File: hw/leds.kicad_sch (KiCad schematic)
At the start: 28 parts, among them Q4 SSM6N35AFE

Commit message: WIP; converging
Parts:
- removed D2101: DONb, LED_SMD:LED_0603_1608Metric, symbol Device:LED
- removed R25: 5k1, Resistor_SMD:R_0603_1608Metric, symbol Device:R_Small
- added D15: LED_Dual_RAG, proj_footprints:LED_Wuerth_Sideview, symbol Device:LED_Dual_KAK
- added R33, R34: 1k, Resistor_SMD:R_0603_1608Metric, symbol Device:R_Small
- D2101: value DONb -> FR_S
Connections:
- net LED_DONb is gone; now on net GND: Q4.4 (S)
- net +3V3: now also D15.2 (A); no longer Q4.5 (G)
- net at Q4.3 (D): now also R34.2
- new net: D15.1 (K1), R33.2
- new net: D15.3 (K2), R34.1
- new net LED_CDON: Q4.5 (G), R33.1
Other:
- note added: "Bi-color LED indicating power and FPGA config. complete: red: power, not configured grn: power, configured"
- moved on the sheet: D7, Q4A, Q4B, R10, R9, R98

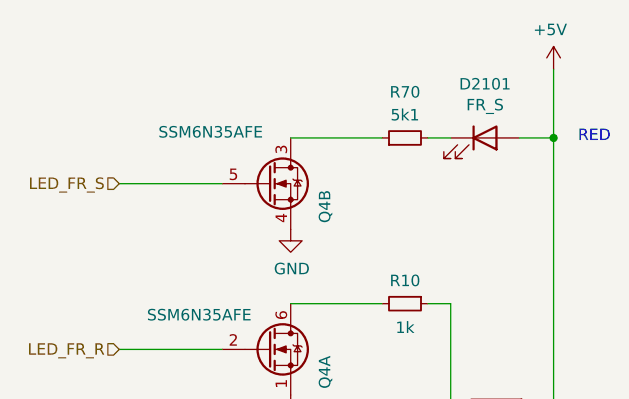
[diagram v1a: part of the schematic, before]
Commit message: updated some component values
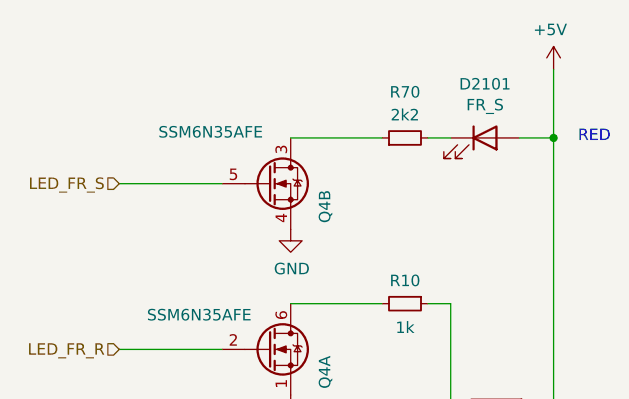
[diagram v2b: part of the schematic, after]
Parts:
- R70: value 5k1 -> 2k2
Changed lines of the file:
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@@
       (effects (font (size 1.27 1.27)))
     )
-    (property "Value" "5k1" (at 187.96 29.845 90)
+    (property "Value" "2k2" (at 187.96 29.845 90)
       (effects (font (size 1.27 1.27)))
     )

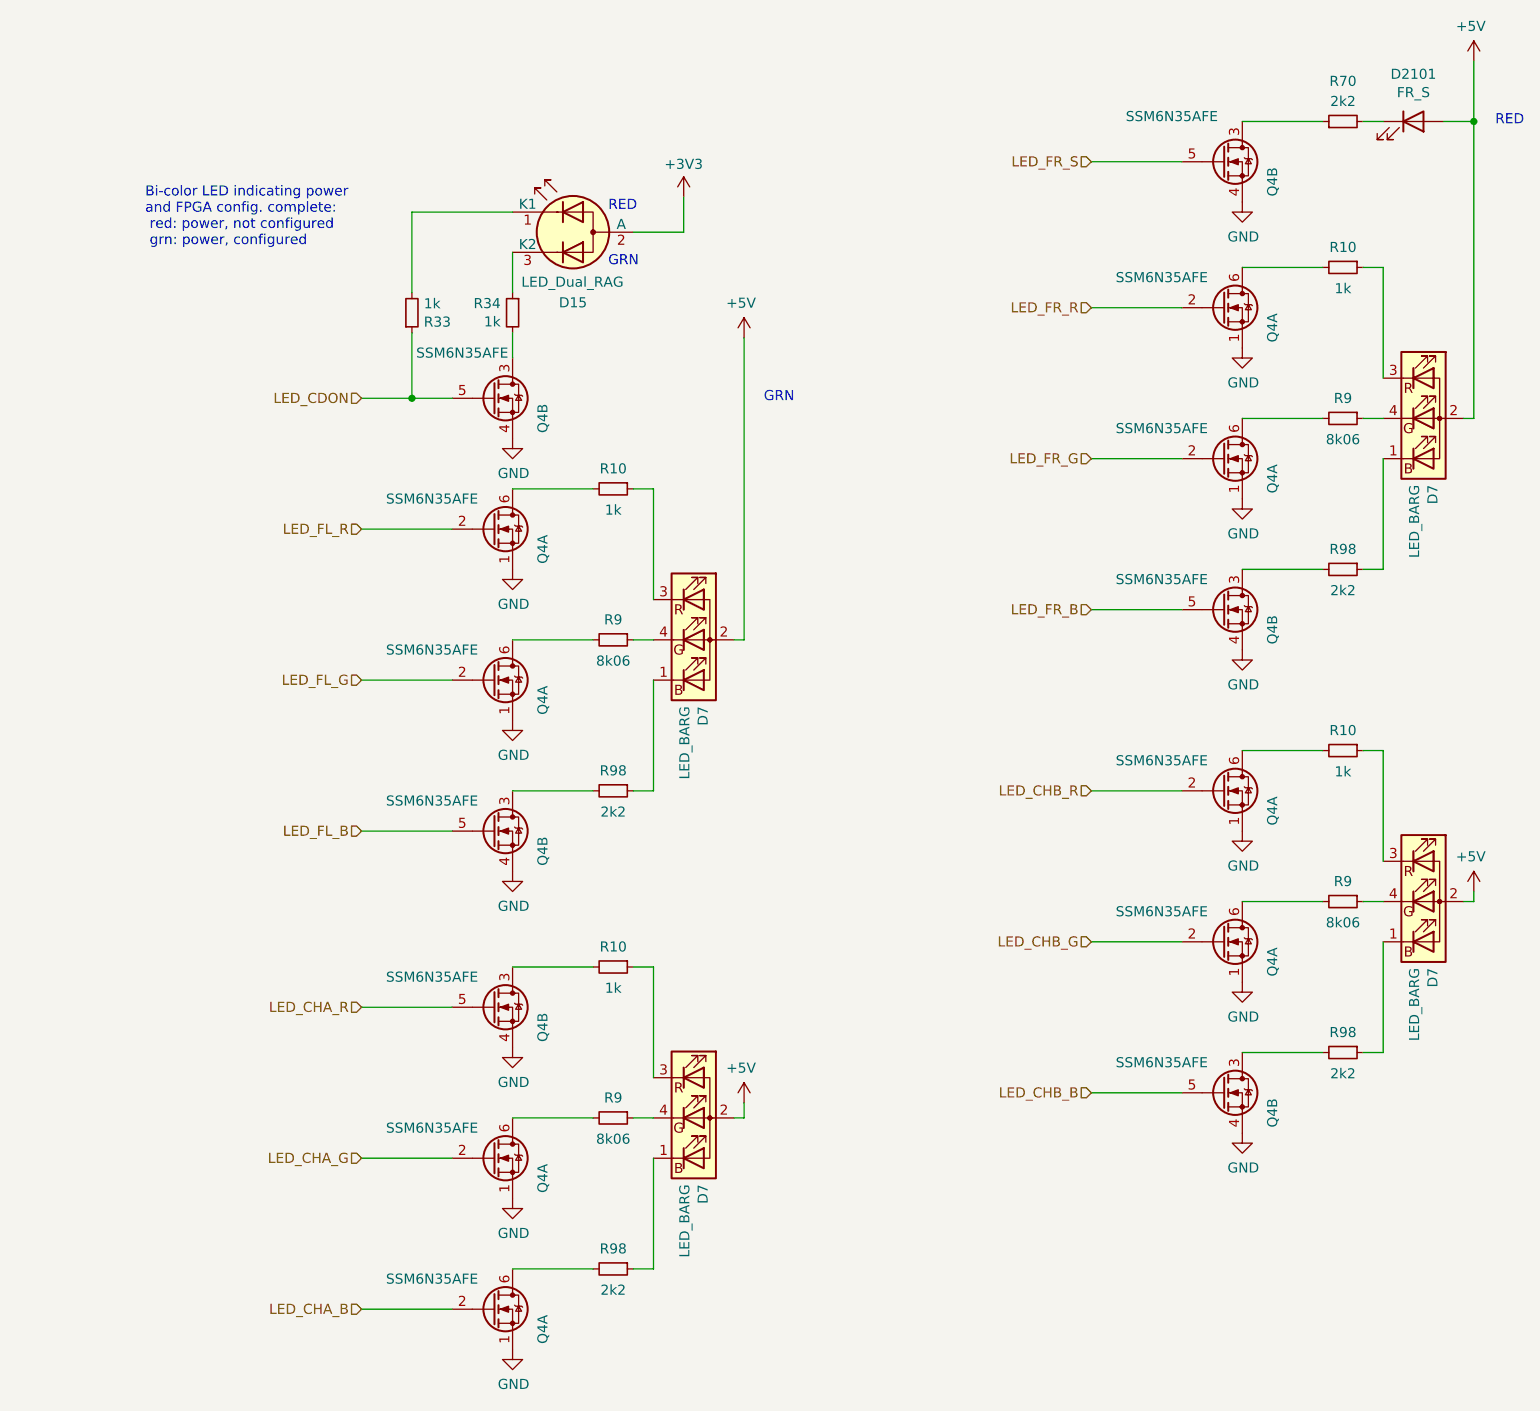
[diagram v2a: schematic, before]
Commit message: Moved LEDs from +5V to 3V3. Removed LED driver FETs.
NOTE: the 3V3 connection is provisional and needs to be
reworked along with the redesign of the 5V net.

The temporary connections exist just to satisfy DRC for now.
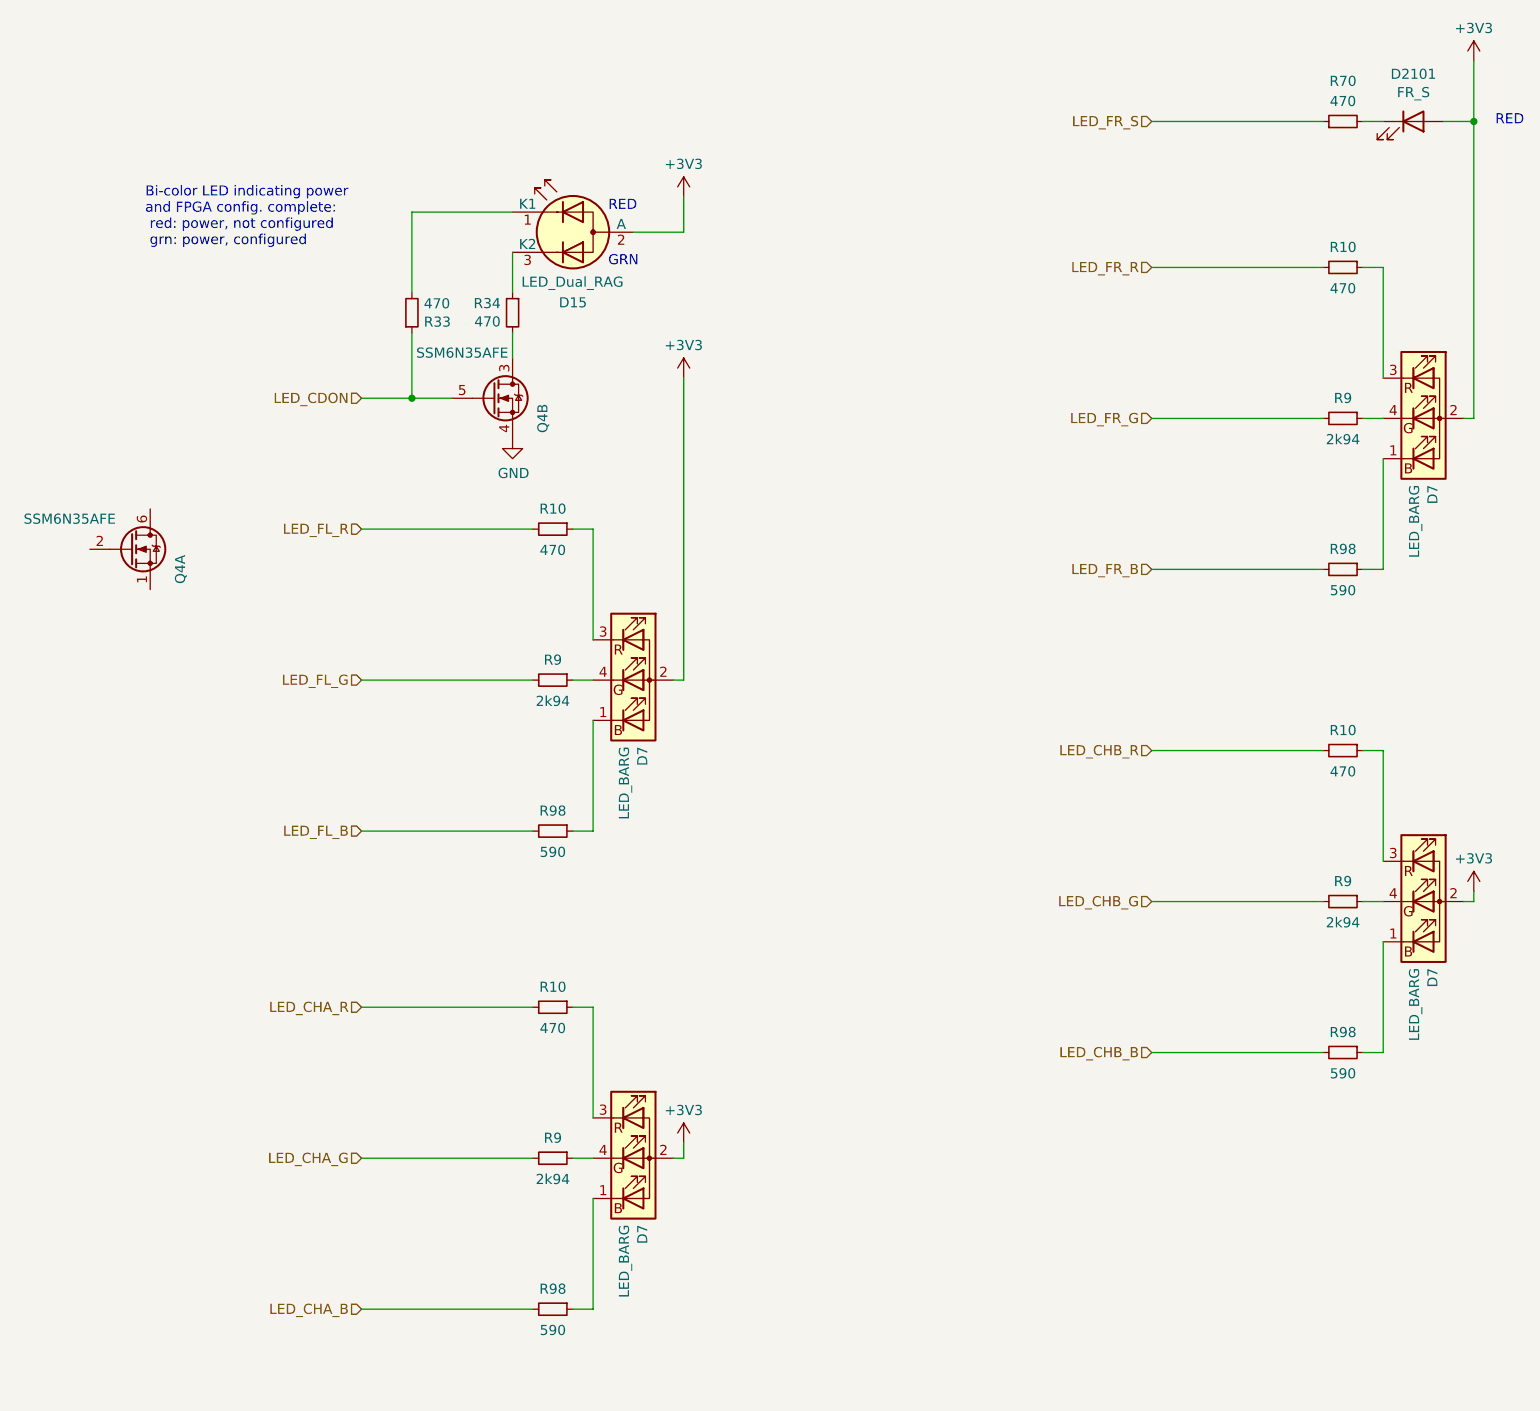
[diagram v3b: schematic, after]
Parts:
- removed Q4 (x7): SSM6N35AFE, proj_footprints:SOT-563-adjusted, symbol Device:Q_Dual_NMOS_S1G1D2S2G2D1
- R10, R33, R34: value 1k -> 470
- R70: value 2k2 -> 470
- R9: value 8k06 -> 2k94
- R98: value 2k2 -> 590
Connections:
- net +5V is gone; now on net +3V3: D2101.2 (A), D7.2 (A), D7.2 (A), D7.2 (A), D7.2 (A)
- net GND: no longer Q4.1 (S)
- net LED_CHA_B: now also R98.2
- net LED_CHA_G: now also R9.2
- net LED_CHA_R: now also R10.2
- net LED_CHB_B: now also R98.2
- net LED_CHB_G: now also R9.2
- net LED_CHB_R: now also R10.2
- net LED_FL_B: now also R98.2
- net LED_FL_G: now also R9.2; no longer Q4.2 (G)
- net LED_FL_R: now also R10.2
- net LED_FR_B: now also R98.2
- net LED_FR_G: now also R9.2
- net LED_FR_R: now also R10.2
- net LED_FR_S: now also R70.1
- net at Q4.6 (D): no longer R9.2
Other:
- moved on the sheet: D7, Q4A, R10, R9, R98

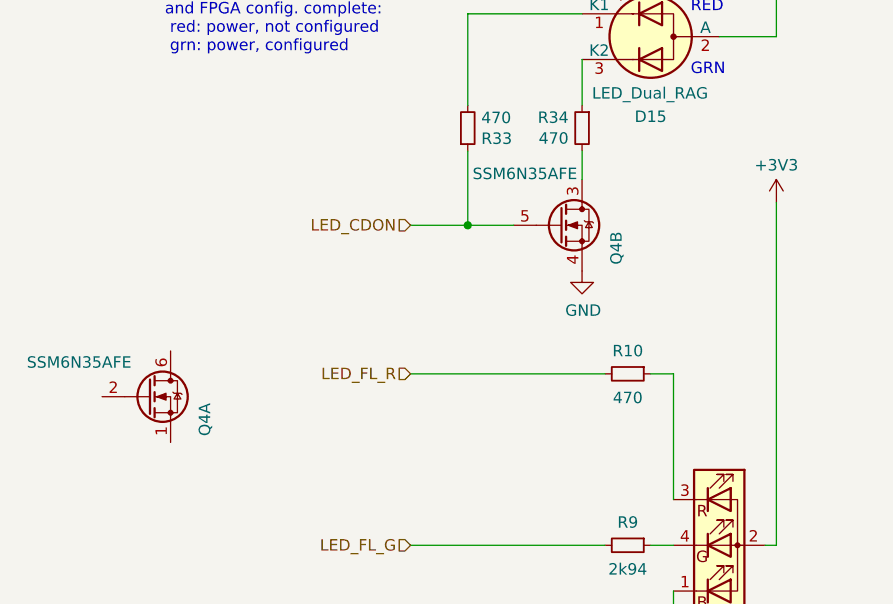
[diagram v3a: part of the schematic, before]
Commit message: [hw] added reset generator; removed 5V fill from FE area!
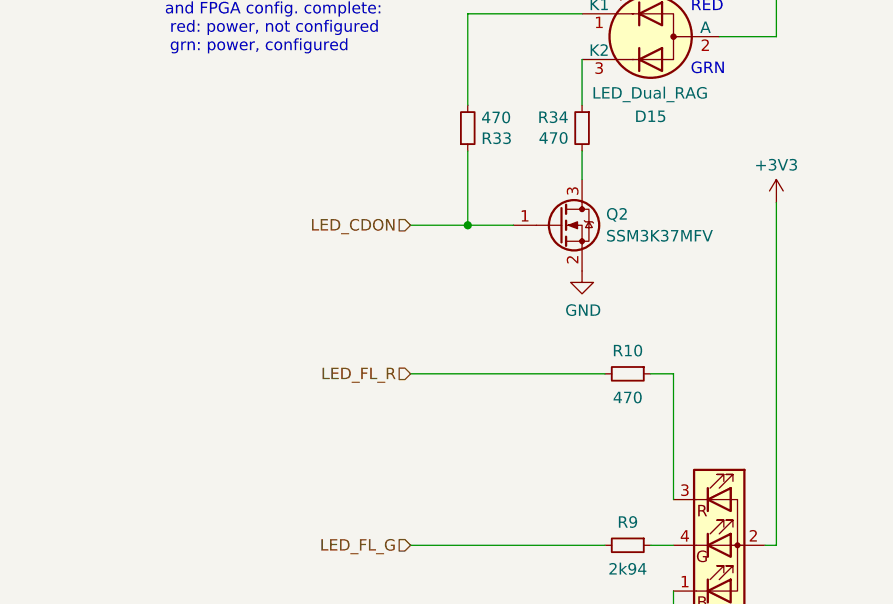
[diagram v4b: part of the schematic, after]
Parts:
- removed Q4: SSM6N35AFE, proj_footprints:SOT-563-adjusted, symbol Device:Q_Dual_NMOS_S1G1D2S2G2D1
- added Q2: SSM3K37MFV, Package_TO_SOT_SMD:SOT-723, symbol Device:Q_NMOS_GSD
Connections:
- net GND: now also Q2.2 (S)
- net LED_CDON: now also Q2.1 (G)
- net at R34.2: now also Q2.3 (D)
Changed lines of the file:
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@@
+    )
+  )
+  (symbol (lib_id "Device:Q_NMOS_GSD") (at 80.645 67.31 0) (unit 1)
+    (in_bom yes) (on_board yes) (dnp no) (fields_autoplaced)
+    (property "Reference" "Q2" (at 85.852 66.0979 0)
+      (effects (font (size 1.27 1.27)) (justify left))
+    )
+    (property "Value" "SSM3K37MFV" (at 85.852 68.5221 0)
+      (effects (font (size 1.27 1.27)) (justify left))
+    )
+    (property "Footprint" "Package_TO_SOT_SMD:SOT-723" (at 85.725 64.77 0)
+      (effects (font (size 1.27 1.27)) hide)
+    )
+    (property "Datasheet" "~" (at 80.645 67.31 0)
+      (effects (font (size 1.27 1.27)) hide)
+    )
+    (property "Manufacturer" "Toshiba" (at 80.645 67.31 0)
+      (effects (font (size 1.27 1.27)) hide)
+    )
+    (property "Part" "SSM3K37MFV" (at 80.645 67.31 0)
+      (effects (font (size 1.27 1.27)) hide)
+    )
+    (pin "3")
+    (pin "2")
+    (pin "1")
+    (instances
+      (project "usbadc"
+        (path "/7c8a1f8d-8834-4c9b-aaae-1f231e9b09a1/33541e06-1943-44ac-875f-55941863f921"
+          (reference "Q2") (unit 1)
+        )
+      )
     )
   )
@@
     )
   )
-  (symbol (lib_id "Device:Q_Dual_NMOS_S1G1D2S2G2D1") (at 34.925 86.36 0) (unit 1)
-    (in_bom yes) (on_board yes) (dnp no)
-    (property "Reference" "Q4" (at 41.275 88.9 90)
-      (effects (font (size 1.27 1.27)))
-    )
-    (property "Value" "SSM6N35AFE" (at 27.305 82.55 0)
-      (effects (font (size 1.27 1.27)))
-    )
-    (property "Footprint" "proj_footprints:SOT-563-adjusted" (at 40.005 86.36 0)
-      (effects (font (size 1.27 1.27)) hide)
-    )
-    (property "Datasheet" "~" (at 40.005 86.36 0)
-      (effects (font (size 1.27 1.27)) hide)
-    )
-    (property "Manufacturer" "Toshiba" (at 34.925 86.36 0)
-      (effects (font (size 1.27 1.27)) hide)
-    )
-    (property "Part" "SSM6N35AFE" (at 34.925 86.36 0)
-      (effects (font (size 1.27 1.27)) hide)
-    )
-    (pin "1")
-    (pin "2")
-    (pin "6")
-    (pin "3")
-    (pin "4")
-    (pin "5")
-    (instances
-      (project "ecevr-proto"
-        (path "/0333b818-5fb1-4de6-9929-c91b1fef8666/00000000-0000-0000-0000-0000621ad2c2"
-          (reference "Q4") (unit 1)
-        )
-      )
-      (project "usbadc"
-        (path "/7c8a1f8d-8834-4c9b-aaae-1f231e9b09a1/33541e06-1943-44ac-875f-55941863f921"
-          (reference "Q6") (unit 1)
-        )
-      )
-    )
-  )
   (symbol (lib_id "power:+3V3") (at 104.775 161.29 0) (unit 1)
     (in_bom yes) (on_board yes) (dnp no) (fields_autoplaced)
@@
         )
       )
-    )
-  )
-  (symbol (lib_id "Device:Q_Dual_NMOS_S1G1D2S2G2D1") (at 80.645 67.31 0) (unit 2)
-    (in_bom yes) (on_board yes) (dnp no)
-    (property "Reference" "Q4" (at 86.995 69.85 90)
-      (effects (font (size 1.27 1.27)))
-    )
-    (property "Value" "SSM6N35AFE" (at 76.835 61.595 0)
-      (effects (font (size 1.27 1.27)))
-    )
-    (property "Footprint" "proj_footprints:SOT-563-adjusted" (at 85.725 67.31 0)
-      (effects (font (size 1.27 1.27)) hide)
-    )
-    (property "Datasheet" "~" (at 85.725 67.31 0)
-      (effects (font (size 1.27 1.27)) hide)
-    )
-    (property "Manufacturer" "Toshiba" (at 80.645 67.31 0)
-      (effects (font (size 1.27 1.27)) hide)
-    )
-    (property "Part" "SSM6N35AFE" (at 80.645 67.31 0)
-      (effects (font (size 1.27 1.27)) hide)
-    )
-    (pin "1")
-    (pin "2")
-    (pin "6")
-    (pin "3")
-    (pin "4")
-    (pin "5")
-    (instances
-      (project "ecevr-proto"
-        (path "/0333b818-5fb1-4de6-9929-c91b1fef8666/00000000-0000-0000-0000-0000621ad2c2"
-          (reference "Q4") (unit 2)
-        )
-      )
-      (project "usbadc"
-        (path "/7c8a1f8d-8834-4c9b-aaae-1f231e9b09a1/33541e06-1943-44ac-875f-55941863f921"
-          (reference "Q6") (unit 2)
-        )
-      )
